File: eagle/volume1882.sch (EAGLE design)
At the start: 27 parts, among them IC1 LM317, IC2 LM337, U1 DS1882, U2 ATMEGA328P_TQFP

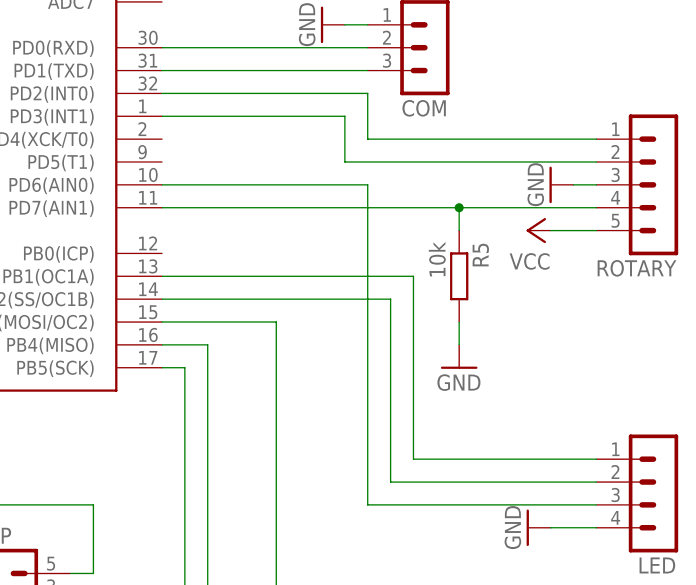
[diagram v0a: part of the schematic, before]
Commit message: output select switch
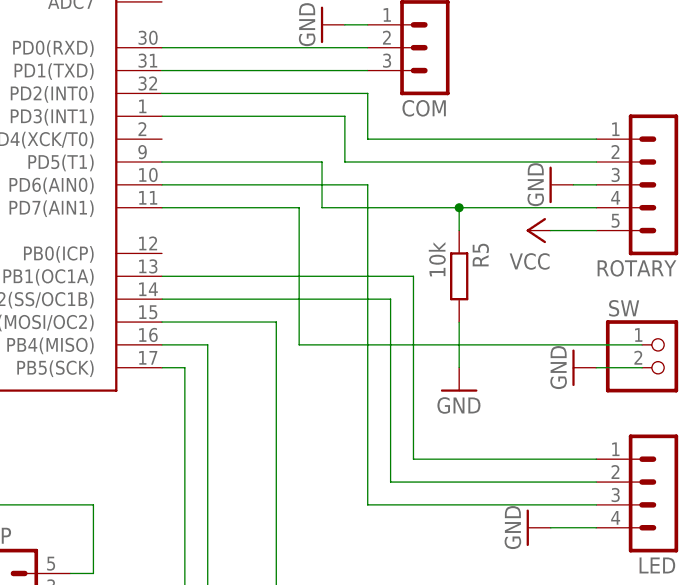
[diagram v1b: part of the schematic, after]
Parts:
- added SW: (no value), pinhead:PINHD-1X2
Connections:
- new net N$25: SW.1, U2.PD7(AIN1)
- net GND: now also SW.2
- net N$11: now also U2.PD5(T1); no longer U2.PD7(AIN1)
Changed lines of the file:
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@@
 <part name="GND22" library="supply1" deviceset="GND" device=""/>
 <part name="P-2" library="supply1" deviceset="V-" device=""/>
+<part name="SW" library="pinhead" deviceset="PINHD-1X2" device=""/>
+<part name="GND23" library="supply1" deviceset="GND" device=""/>
 </parts>
 <sheets>
@@
 <instance part="ROTARY" gate="G$1" x="254" y="60.96" rot="R180"/>
 <instance part="GND9" gate="1" x="241.3" y="60.96" rot="R270"/>
-<instance part="GND10" gate="1" x="231.14" y="40.64"/>
+<instance part="GND10" gate="1" x="231.14" y="38.1"/>
 <instance part="R5" gate="G$1" x="231.14" y="50.8" rot="R270"/>
 <instance part="P+9" gate="VCC" x="238.76" y="55.88" rot="R90"/>
@@
 <instance part="GND22" gate="1" x="86.36" y="124.46"/>
 <instance part="P-2" gate="1" x="109.22" y="157.48" rot="R90"/>
+<instance part="SW" gate="G$1" x="254" y="40.64"/>
+<instance part="GND23" gate="1" x="243.84" y="40.64" rot="R270"/>
 </instances>
 <busses>
@@
 <pinref part="R5" gate="G$1" pin="2"/>
 <pinref part="GND10" gate="1" pin="GND"/>
-<wire x1="231.14" y1="45.72" x2="231.14" y2="43.18" width="0.1524" layer="91"/>
+<wire x1="231.14" y1="45.72" x2="231.14" y2="40.64" width="0.1524" layer="91"/>
 </segment>
 <segment>
@@
 <pinref part="GND22" gate="1" pin="GND"/>
 <wire x1="86.36" y1="129.54" x2="86.36" y2="127" width="0.1524" layer="91"/>
+</segment>
+<segment>
+<pinref part="SW" gate="G$1" pin="2"/>
+<pinref part="GND23" gate="1" pin="GND"/>
+<wire x1="251.46" y1="40.64" x2="246.38" y2="40.64" width="0.1524" layer="91"/>
 </segment>
 </net>
@@
 <net name="N$11" class="0">
 <segment>
-<pinref part="U2" gate="U$1" pin="PD7(AIN1)"/>
 <pinref part="ROTARY" gate="G$1" pin="4"/>
-<wire x1="198.12" y1="58.42" x2="231.14" y2="58.42" width="0.1524" layer="91"/>
 <pinref part="R5" gate="G$1" pin="1"/>
 <wire x1="231.14" y1="58.42" x2="246.38" y2="58.42" width="0.1524" layer="91"/>
 <wire x1="231.14" y1="55.88" x2="231.14" y2="58.42" width="0.1524" layer="91"/>
+<pinref part="U2" gate="U$1" pin="PD5(T1)"/>
+<wire x1="198.12" y1="63.5" x2="215.9" y2="63.5" width="0.1524" layer="91"/>
+<wire x1="215.9" y1="63.5" x2="215.9" y2="58.42" width="0.1524" layer="91"/>
+<wire x1="215.9" y1="58.42" x2="231.14" y2="58.42" width="0.1524" layer="91"/>
 <junction x="231.14" y="58.42"/>
 </segment>
@@
 </segment>
 </net>
+<net name="N$25" class="0">
+<segment>
+<pinref part="U2" gate="U$1" pin="PD7(AIN1)"/>
+<wire x1="198.12" y1="58.42" x2="213.36" y2="58.42" width="0.1524" layer="91"/>
+<wire x1="213.36" y1="58.42" x2="213.36" y2="43.18" width="0.1524" layer="91"/>
+<pinref part="SW" gate="G$1" pin="1"/>
+<wire x1="213.36" y1="43.18" x2="251.46" y2="43.18" width="0.1524" layer="91"/>
+</segment>
+</net>

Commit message: finished board
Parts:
- added +7V, -7V, GND: TPTP12SQ, testpad:TPTP12SQ
- added H1, H2, H3: MOUNT-PAD-ROUND3.0, holes:MOUNT-PAD-ROUND3.0
- added R10, R11, R12: 470R, resistor:R-EU_R1206
- added R9: 10k, resistor:R-EU_R1206
- added RELAY: (no value), con-lstb:MA03-1
- renumbered PWR to POWER
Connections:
- new net N$23: R9.1, SW.2, U2.PD5(T1)
- new net N$26: LED.1, R10.2
- new net N$27: LED.2, R11.2
- new net N$28: LED.3, R12.2
- net GND: now also C6.+, C7.+, GND.TP, R9.2, RELAY.3; no longer C6.-, C7.-, SW.2
- net N$11: now also U2.PD4(XCK/T0); no longer U2.PD5(T1)
- net N$13: now also R11.1; no longer LED.1
- net N$14: now also R10.1; no longer LED.2
- net N$15: now also R12.1; no longer LED.3
- net N$21: now also C6.-; no longer C6.+
- net N$25: now also RELAY.1, U2.PC2(ADC2); no longer SW.1, U2.PD7(AIN1)
- net V+: now also +7V.TP
- net V-: now also -7V.TP, C7.-; no longer C7.+
- net VCC: now also RELAY.2, SW.1
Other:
- moved on the sheet: C6, C7, SW
